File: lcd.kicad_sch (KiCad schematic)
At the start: 2 parts, among them J1 687110149022, J2 687140149022

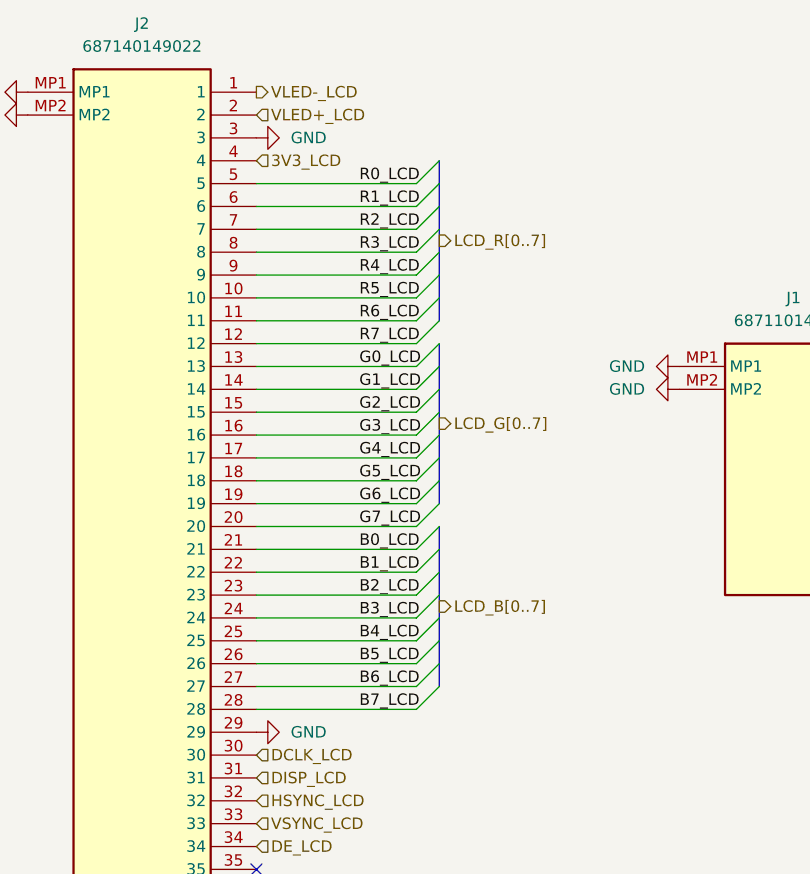
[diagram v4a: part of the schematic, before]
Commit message: Fix some ERC errors
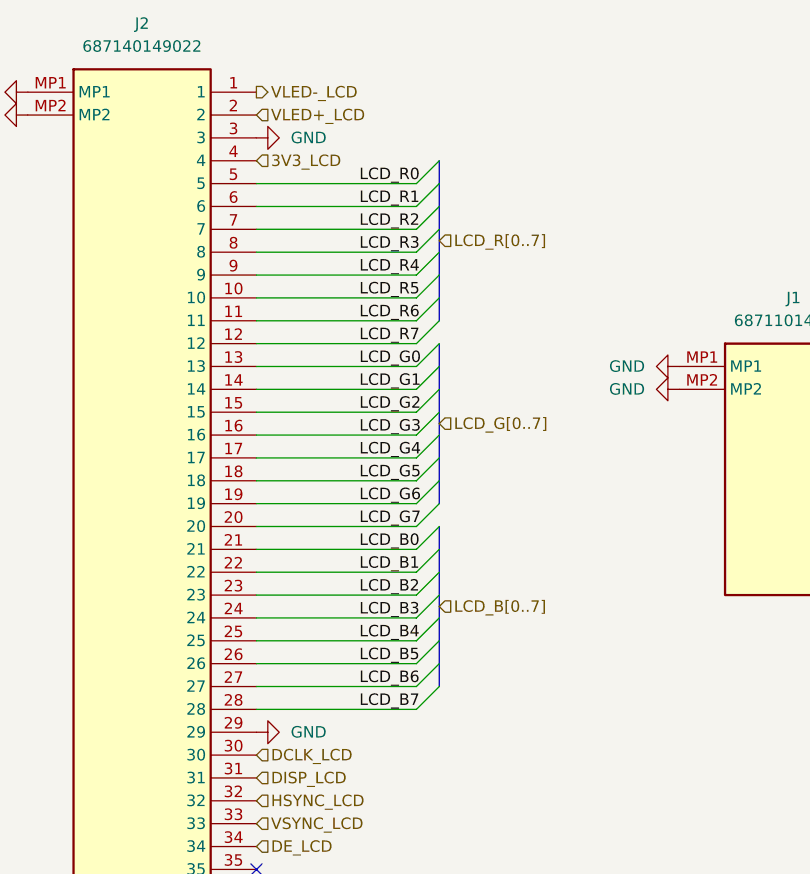
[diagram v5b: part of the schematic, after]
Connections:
- net B0_LCD renamed LCD_B0
- net B1_LCD renamed LCD_B1
- net B2_LCD renamed LCD_B2
- net B3_LCD renamed LCD_B3
- net B4_LCD renamed LCD_B4
- net B5_LCD renamed LCD_B5
- net B6_LCD renamed LCD_B6
- net B7_LCD renamed LCD_B7
- net G0_LCD renamed LCD_G0
- net G1_LCD renamed LCD_G1
- net G2_LCD renamed LCD_G2
- net G3_LCD renamed LCD_G3
- net G4_LCD renamed LCD_G4
- net G5_LCD renamed LCD_G5
- net G6_LCD renamed LCD_G6
- net G7_LCD renamed LCD_G7
- net R0_LCD renamed LCD_R0
- net R1_LCD renamed LCD_R1
- net R2_LCD renamed LCD_R2
- net R3_LCD renamed LCD_R3
- net R4_LCD renamed LCD_R4
- net R5_LCD renamed LCD_R5
- net R6_LCD renamed LCD_R6
- net R7_LCD renamed LCD_R7
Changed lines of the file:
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@@
 		)
 	)
-	(label "R3_LCD"
+	(label "LCD_R3"
 		(at 129.54 66.04 0)
 		(effects
@@
 		)
 	)
-	(label "R1_LCD"
+	(label "LCD_B2"
+		(at 129.54 104.14 0)
+		(effects
+			(font
+				(size 1.27 1.27)
+			)
+			(justify left bottom)
+		)
+	)
+	(label "LCD_B0"
+		(at 129.54 99.06 0)
+		(effects
+			(font
+				(size 1.27 1.27)
+			)
+			(justify left bottom)
+		)
+	)
+	(label "LCD_B1"
+		(at 129.54 101.6 0)
+		(effects
+			(font
+				(size 1.27 1.27)
+			)
+			(justify left bottom)
+		)
+	)
+	(label "LCD_B6"
+		(at 129.54 114.3 0)
+		(effects
+			(font
+				(size 1.27 1.27)
+			)
+			(justify left bottom)
+		)
+	)
+	(label "LCD_R1"
 		(at 129.54 60.96 0)
 		(effects
@@
 		)
 	)
-	(label "G7_LCD"
+	(label "LCD_R4"
+		(at 129.54 68.58 0)
+		(effects
+			(font
+				(size 1.27 1.27)
+			)
+			(justify left bottom)
+		)
+	)
+	(label "LCD_R6"
+		(at 129.54 73.66 0)
+		(effects
+			(font
+				(size 1.27 1.27)
+			)
+			(justify left bottom)
+		)
+	)
+	(label "LCD_G1"
+		(at 129.54 81.28 0)
+		(effects
+			(font
+				(size 1.27 1.27)
+			)
+			(justify left bottom)
+		)
+	)
+	(label "LCD_G5"
+		(at 129.54 91.44 0)
+		(effects
+			(font
+				(size 1.27 1.27)
+			)
+			(justify left bottom)
+		)
+	)
+	(label "LCD_G7"
 		(at 129.54 96.52 0)
 		(effects
@@
 		)
 	)
-	(label "R2_LCD"
+	(label "LCD_B4"
+		(at 129.54 109.22 0)
+		(effects
+			(font
+				(size 1.27 1.27)
+			)
+			(justify left bottom)
+		)
+	)
+	(label "LCD_G0"
+		(at 129.54 78.74 0)
+		(effects
+			(font
+				(size 1.27 1.27)
+			)
+			(justify left bottom)
+		)
+	)
+	(label "LCD_B7"
+		(at 129.54 116.84 0)
+		(effects
+			(font
+				(size 1.27 1.27)
+			)
+			(justify left bottom)
+		)
+	)
+	(label "LCD_G6"
+		(at 129.54 93.98 0)
+		(effects
+			(font
+				(size 1.27 1.27)
+			)
+			(justify left bottom)
+		)
+	)
+	(label "LCD_R7"
+		(at 129.54 76.2 0)
+		(effects
+			(font
+				(size 1.27 1.27)
+			)
+			(justify left bottom)
+		)
+	)
+	(label "LCD_R2"
 		(at 129.54 63.5 0)
 		(effects
@@
 		)
 	)
-	(label "G4_LCD"
+	(label "LCD_B3"
+		(at 129.54 106.68 0)
+		(effects
+			(font
+				(size 1.27 1.27)
+			)
+			(justify left bottom)
+		)
+	)
+	(label "LCD_B5"
+		(at 129.54 111.76 0)
+		(effects
+			(font
+				(size 1.27 1.27)
+			)
+			(justify left bottom)
+		)
+	)
+	(label "LCD_R5"
+		(at 129.54 71.12 0)
+		(effects
+			(font
+				(size 1.27 1.27)
+			)
+			(justify left bottom)
+		)
+	)
+	(label "LCD_R0"
+		(at 129.54 58.42 0)
+		(effects
+			(font
+				(size 1.27 1.27)
+			)
+			(justify left bottom)
+		)
+	)
+	(label "LCD_G4"
 		(at 129.54 88.9 0)
 		(effects
@@
 		)
 	)
-	(label "G6_LCD"
-		(at 129.54 93.98 0)
-		(effects
-			(font
-				(size 1.27 1.27)
-			)
-			(justify left bottom)
-		)
-	)
-	(label "R0_LCD"
-		(at 129.54 58.42 0)
-		(effects
-			(font
-				(size 1.27 1.27)
-			)
-			(justify left bottom)
-		)
-	)
-	(label "B0_LCD"
-		(at 129.54 99.06 0)
-		(effects
-			(font
-				(size 1.27 1.27)
-			)
-			(justify left bottom)
-		)
-	)
-	(label "G5_LCD"
-		(at 129.54 91.44 0)
-		(effects
-			(font
-				(size 1.27 1.27)
-			)
-			(justify left bottom)
-		)
-	)
-	(label "G2_LCD"
+	(label "LCD_G3"
+		(at 129.54 86.36 0)
+		(effects
+			(font
+				(size 1.27 1.27)
+			)
+			(justify left bottom)
+		)
+	)
+	(label "LCD_G2"
 		(at 129.54 83.82 0)
-		(effects
-			(font
-				(size 1.27 1.27)
-			)
-			(justify left bottom)
-		)
-	)
-	(label "B2_LCD"
-		(at 129.54 104.14 0)
-		(effects
-			(font
-				(size 1.27 1.27)
-			)
-			(justify left bottom)
-		)
-	)
-	(label "R5_LCD"
-		(at 129.54 71.12 0)
-		(effects
-			(font
-				(size 1.27 1.27)
-			)
-			(justify left bottom)
-		)
-	)
-	(label "B5_LCD"
-		(at 129.54 111.76 0)
-		(effects
-			(font
-				(size 1.27 1.27)
-			)
-			(justify left bottom)
-		)
-	)
-	(label "B4_LCD"
-		(at 129.54 109.22 0)
-		(effects
-			(font
-				(size 1.27 1.27)
-			)
-			(justify left bottom)
-		)
-	)
-	(label "G0_LCD"
-		(at 129.54 78.74 0)
-		(effects
-			(font
-				(size 1.27 1.27)
-			)
-			(justify left bottom)
-		)
-	)
-	(label "G3_LCD"
-		(at 129.54 86.36 0)
-		(effects
-			(font
-				(size 1.27 1.27)
-			)
-			(justify left bottom)
-		)
-	)
-	(label "R6_LCD"
-		(at 129.54 73.66 0)
-		(effects
-			(font
-				(size 1.27 1.27)
-			)
-			(justify left bottom)
-		)
-	)
-	(label "B1_LCD"
-		(at 129.54 101.6 0)
-		(effects
-			(font
-				(size 1.27 1.27)
-			)
-			(justify left bottom)
-		)
-	)
-	(label "R7_LCD"
-		(at 129.54 76.2 0)
-		(effects
-			(font
-				(size 1.27 1.27)
-			)
-			(justify left bottom)
-		)
-	)
-	(label "R4_LCD"
-		(at 129.54 68.58 0)
-		(effects
-			(font
-				(size 1.27 1.27)
-			)
-			(justify left bottom)
-		)
-	)
-	(label "B6_LCD"
-		(at 129.54 114.3 0)
-		(effects
-			(font
-				(size 1.27 1.27)
-			)
-			(justify left bottom)
-		)
-	)
-	(label "G1_LCD"
-		(at 129.54 81.28 0)
-		(effects
-			(font
-				(size 1.27 1.27)
-			)
-			(justify left bottom)
-		)
-	)
-	(label "B3_LCD"
-		(at 129.54 106.68 0)
-		(effects
-			(font
-				(size 1.27 1.27)
-			)
-			(justify left bottom)
-		)
-	)
-	(label "B7_LCD"
-		(at 129.54 116.84 0)
 		(effects
 			(font
@@
 	)
 	(hierarchical_label "LCD_R[0..7]"
-		(shape output)
+		(shape input)
 		(at 138.43 64.77 0)
 		(effects
@@
 	)
 	(hierarchical_label "LCD_G[0..7]"
-		(shape output)
+		(shape input)
 		(at 138.43 85.09 0)
 		(effects
@@
 	)
 	(hierarchical_label "LCD_B[0..7]"
-		(shape output)
+		(shape input)
 		(at 138.43 105.41 0)
 		(effects

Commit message: Fix warnings for footprint
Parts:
- J1: footprint 687110149022 -> weather-station-poc-fp:687110149022
- J2: footprint 687140149022 -> weather-station-poc-fp:687140149022
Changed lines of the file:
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@@
 			)
 		)
-		(property "Footprint" "687140149022"
+		(property "Footprint" "weather-station-poc-fp:687140149022"
 			(at 114.3 143.18 0)
 			(effects
@@
 			)
 		)
-		(property "Footprint" "687110149022"
+		(property "Footprint" "weather-station-poc-fp:687110149022"
 			(at 186.69 173.66 0)
 			(effects

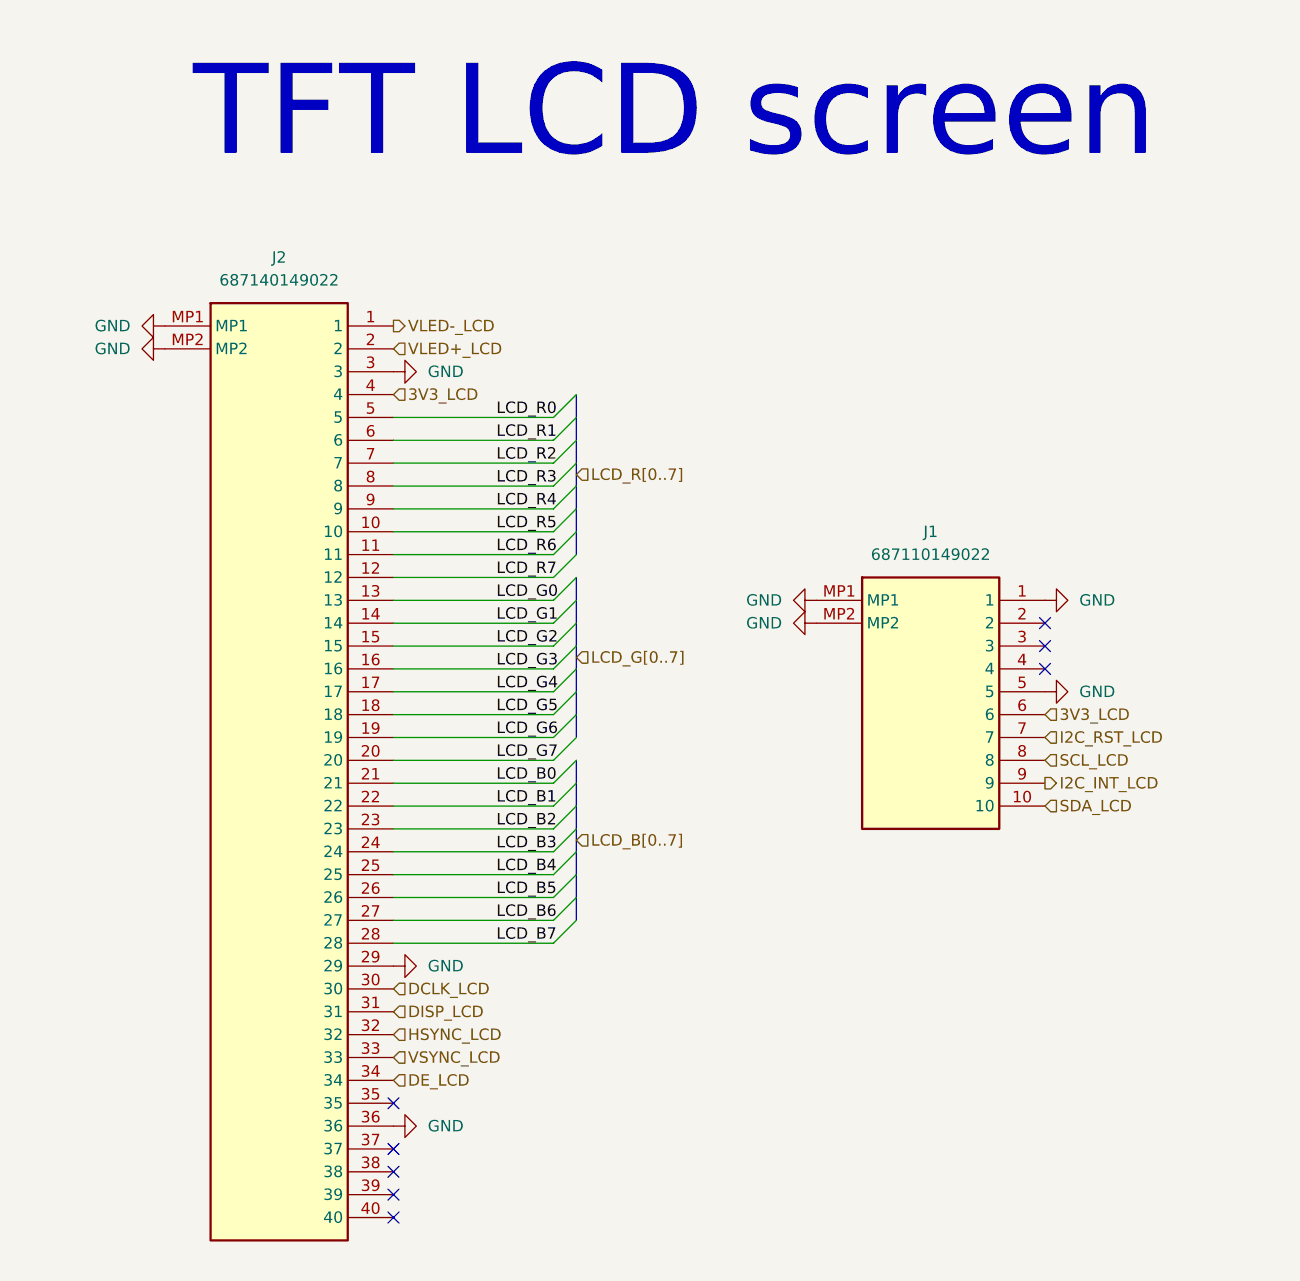
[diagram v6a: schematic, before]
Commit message: Functionnal block delimiting in schematics
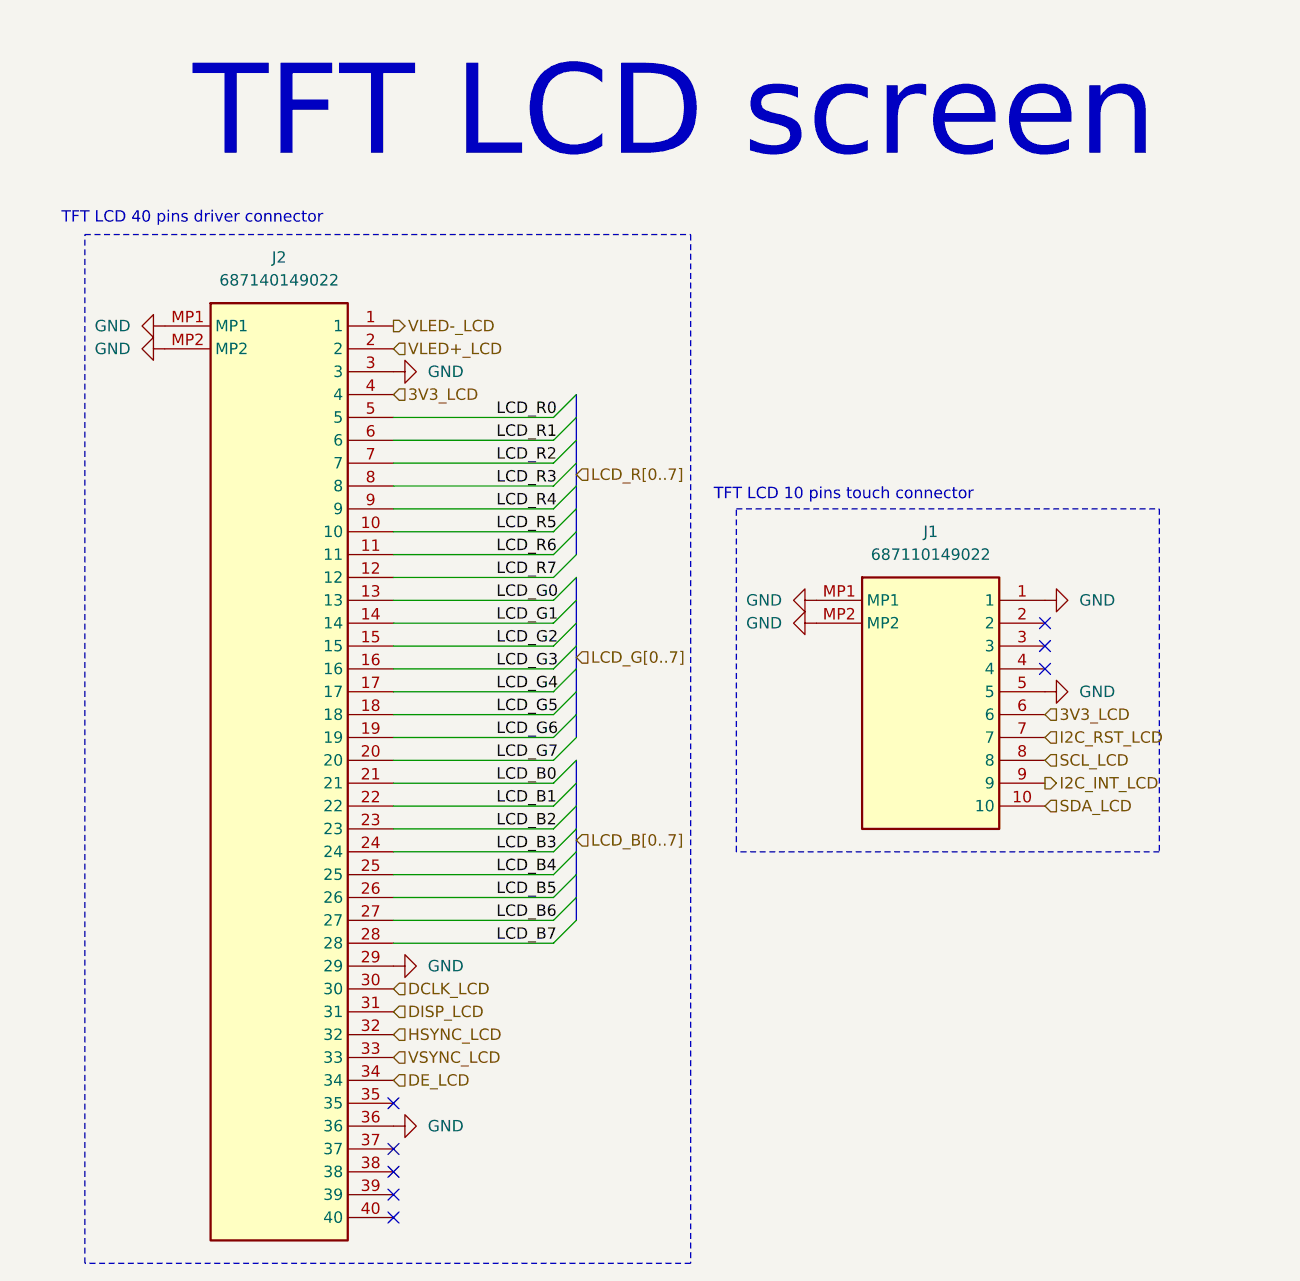
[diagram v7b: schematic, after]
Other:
- note added: "TFT LCD 10 pins touch connector"
- note added: "TFT LCD 40 pins driver connector"
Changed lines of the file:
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@@
 	(generator_version "9.0")
 	(paper "A4")
+	(rectangle
+		(start 83.82 38.1)
+		(end 151.13 152.4)
+		(stroke
+			(width 0)
+			(type dash)
+		)
+		(fill
+			(type none)
+		)
+	)
+	(rectangle
+		(start 156.21 68.58)
+		(end 203.2 106.68)
+		(stroke
+			(width 0)
+			(type dash)
+		)
+		(fill
+			(type none)
+		)
+	)
+	(text "TFT LCD 40 pins driver connector"
+		(exclude_from_sim no)
+		(at 95.758 36.322 0)
+		(effects
+			(font
+				(size 1.27 1.27)
+			)
+		)
+	)
+	(text "TFT LCD 10 pins touch connector"
+		(exclude_from_sim no)
+		(at 168.148 67.056 0)
+		(effects
+			(font
+				(size 1.27 1.27)
+			)
+		)
+	)
 	(text "TFT LCD screen"
 		(exclude_from_sim no)

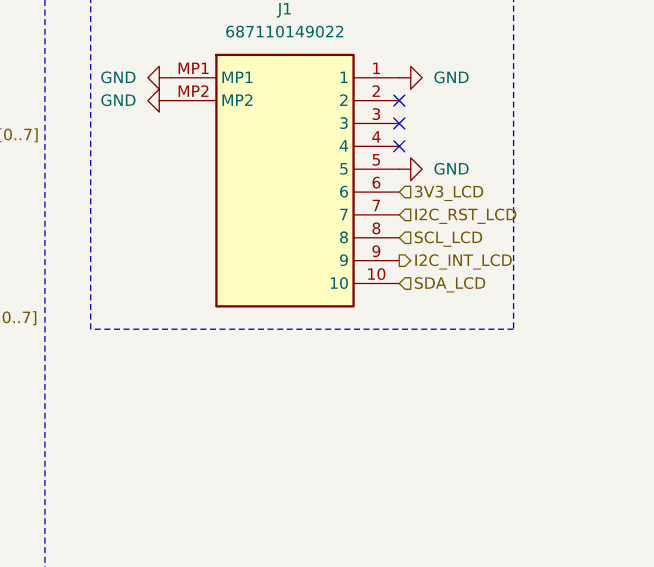
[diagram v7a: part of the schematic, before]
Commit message: Reorganise synoptic schematic for better reading Closes #26
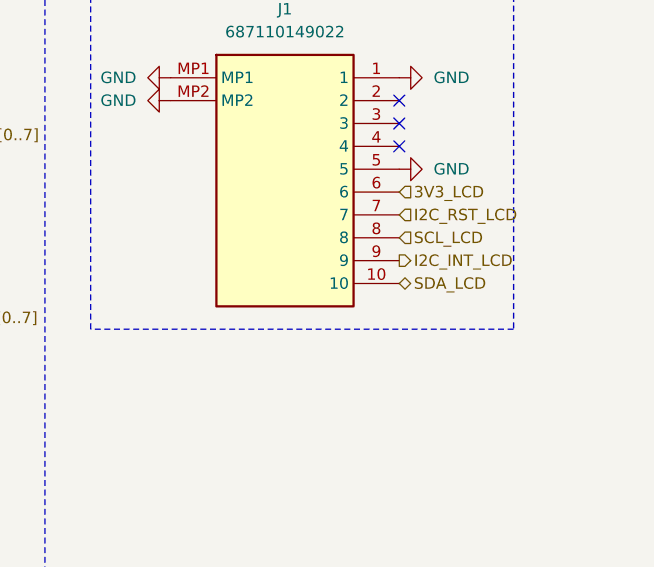
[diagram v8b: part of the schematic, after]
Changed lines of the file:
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@@
 	)
 	(hierarchical_label "SDA_LCD"
-		(shape input)
+		(shape bidirectional)
 		(at 190.5 101.6 0)
 		(effects
